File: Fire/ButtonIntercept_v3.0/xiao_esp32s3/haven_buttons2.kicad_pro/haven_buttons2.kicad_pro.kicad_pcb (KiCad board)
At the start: 2 copper layers, 56 x 92 mm, 56 parts, among them J1 Conn_01x07_Socket, J2 Conn_01x07_Socket, J3 Screw_Terminal_01x04, J4 Screw_Terminal_01x04, J6 Screw_Terminal_01x04, J7 Screw_Terminal_01x04, J8 Screw_Terminal_01x02, J9 Screw_Terminal_01x04, Q1 BC817, Q2 BC817, Q3 BC817, Q4 BC817, Q5 BC817, Q6 BC817, Q7 BC817, Q8 BC817, SW1 SW_DIP_x03, U2 PCA9555PW, U21 TLV1117-50IDCYR

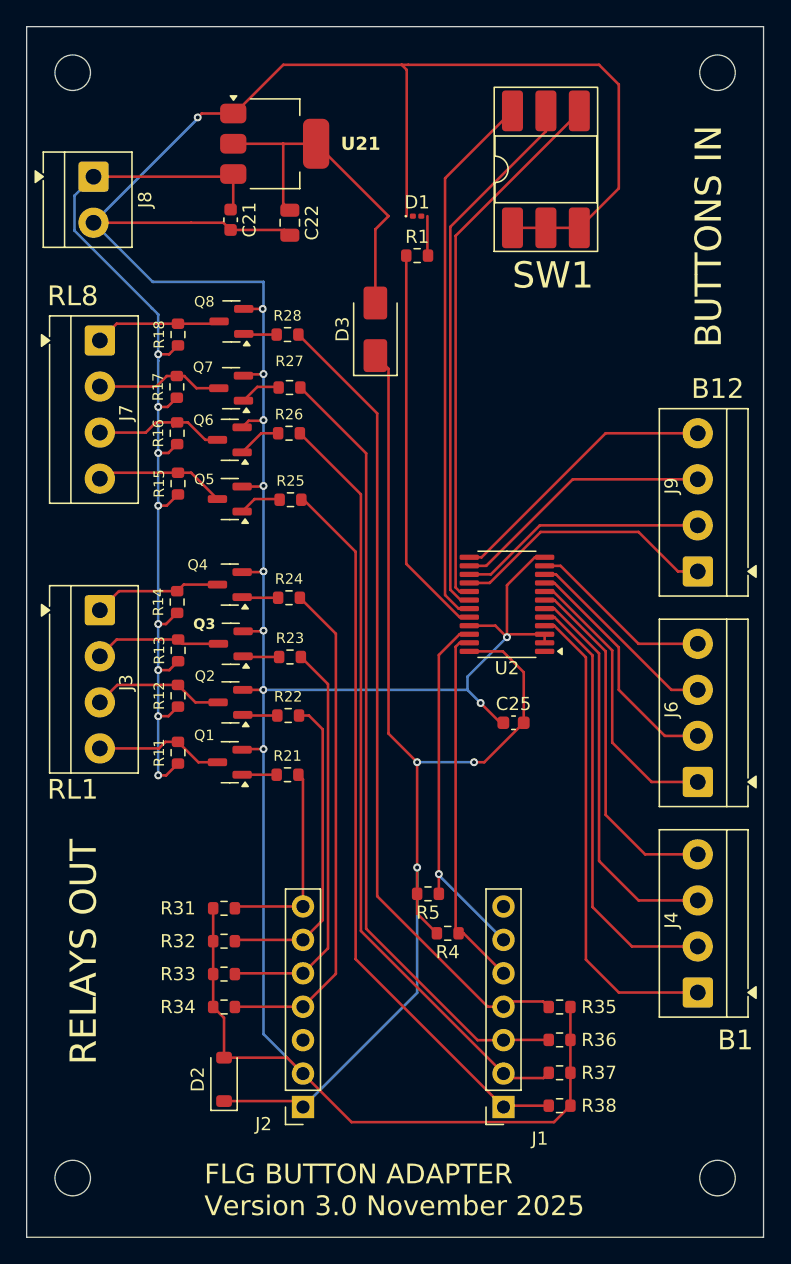
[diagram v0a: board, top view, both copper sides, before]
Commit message: adding files for buttons v3 manufacturing
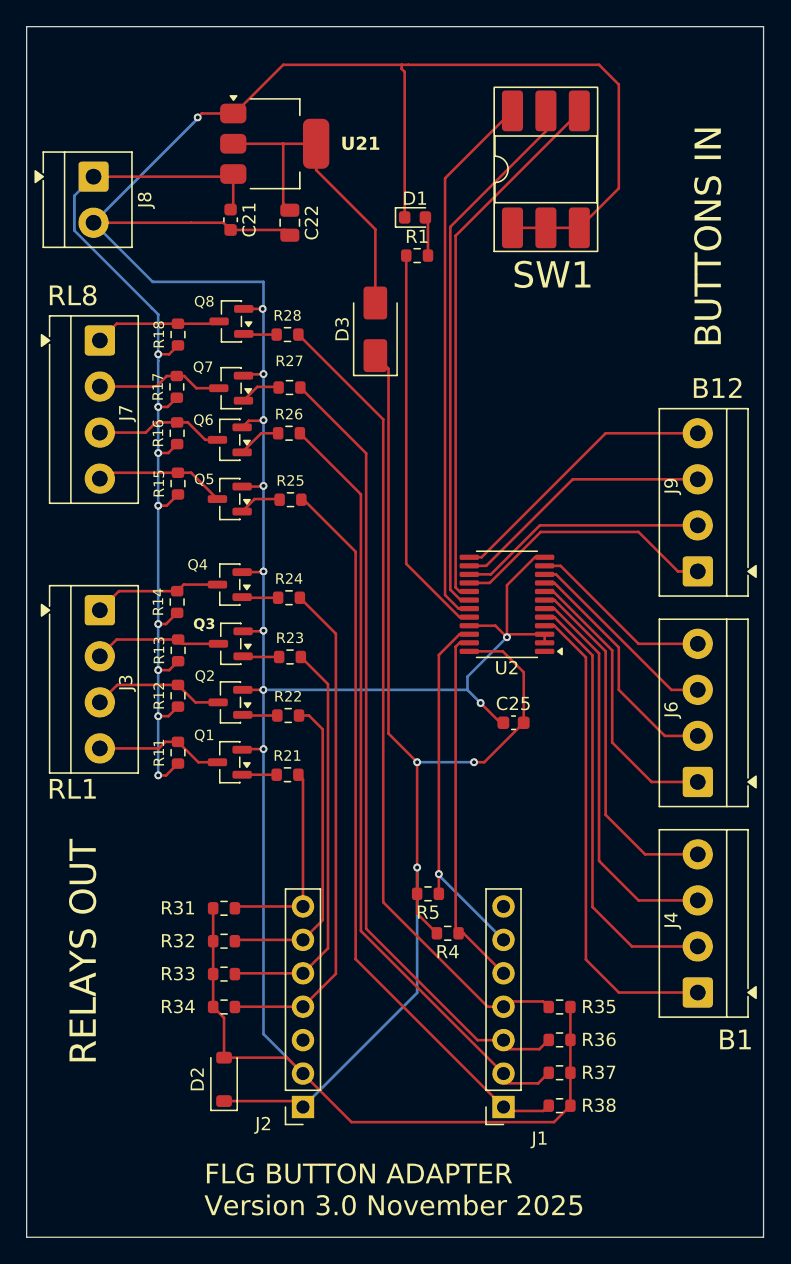
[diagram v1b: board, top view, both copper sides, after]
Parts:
- removed H1, H2, H3, H4: MountingHole, MountingHole:MountingHole_2.7mm_M2.5
- D1: footprint LED_SMD:LED_0201_0603Metric -> LED_SMD:LED_0603_1608Metric
- moved D1 0.18 mm to (84.0, 59.0)
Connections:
- J1 pad 1: /OUT 8 -> /OUT 5
- J1 pad 2: /OUT 7 -> /OUT 6
- J1 pad 3: /OUT 6 -> /OUT 7
- J1 pad 4: /OUT 5 -> /OUT 8
- R35 pad 2: /OUT 5 -> /OUT 8
- R36 pad 2: /OUT 6 -> /OUT 7
- R37 pad 2: /OUT 7 -> /OUT 6
- R38 pad 2: /OUT 8 -> /OUT 5
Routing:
- net /OUT 7: track 60.5 -> 61.6 mm
- net /OUT 6: track 58.7 -> 59.7 mm
- net Net-(D3-A): track 26.3 -> 25.5 mm
